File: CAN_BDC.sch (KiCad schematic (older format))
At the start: 27 parts, among them P1 CONN_01X02, P2 CONN_01X05, P3 CONN_01X02, P4 CONN_01X04, P5 CONN_01X04, P6 CONN_01X02, P7 CONN_01X04, P8 CONN_01X04, P9 CONN_01X02, U1 PSD2CAN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

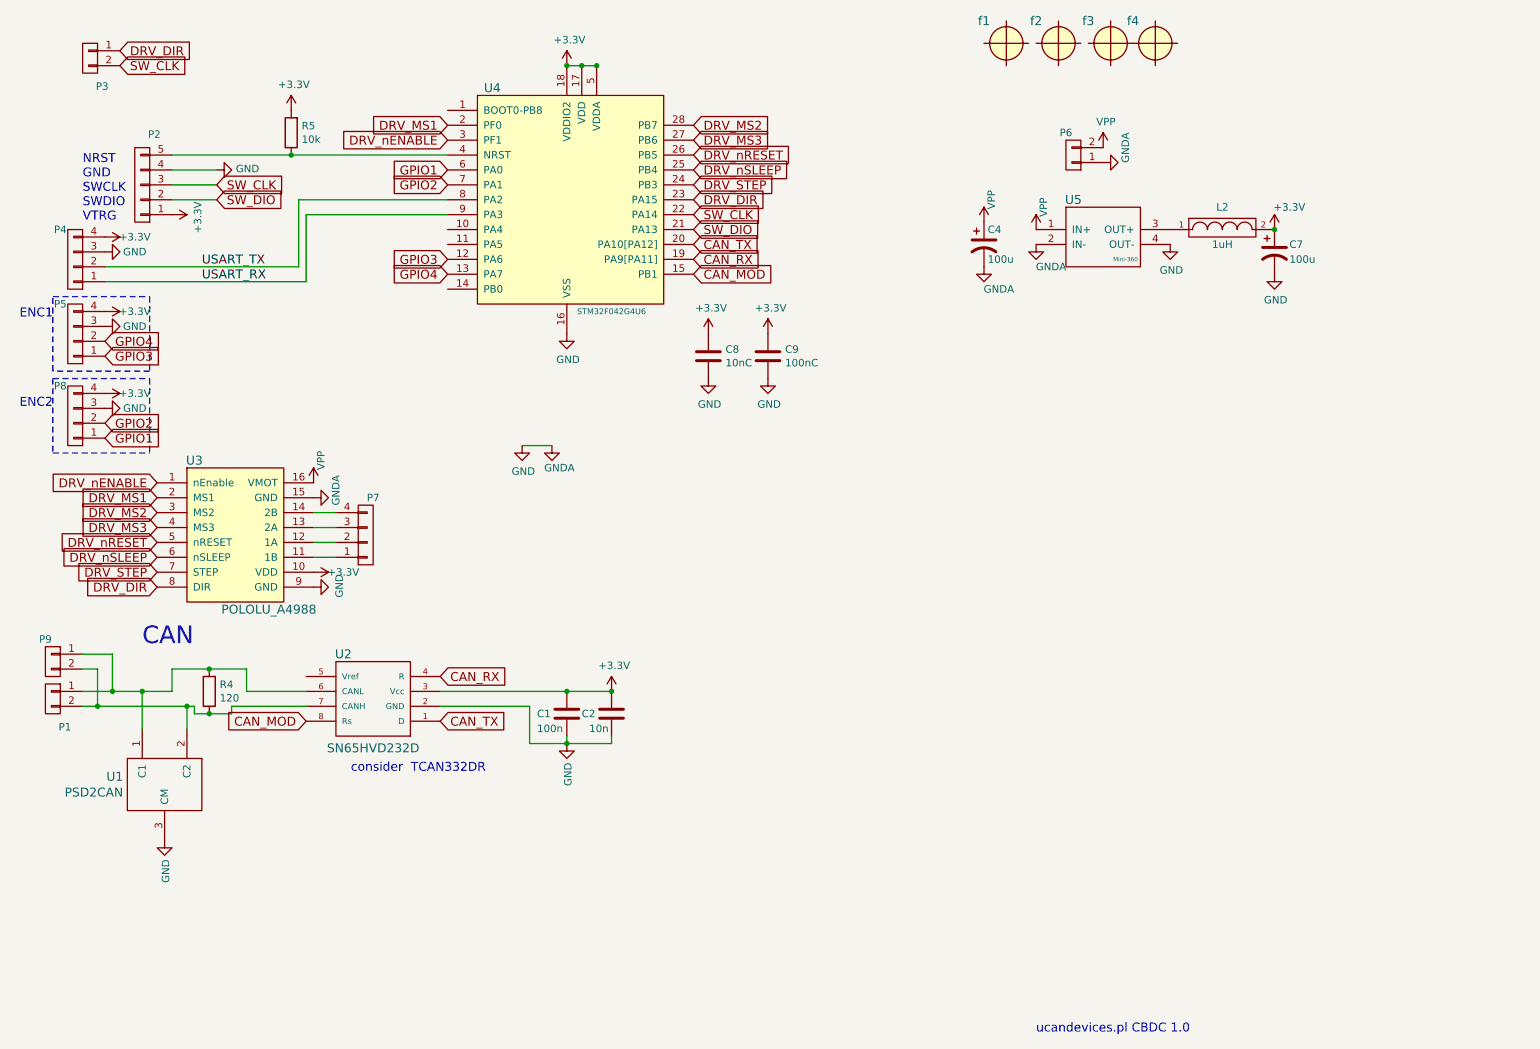
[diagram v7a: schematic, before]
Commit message: DRV8825 and DRV8801 solder pads addition
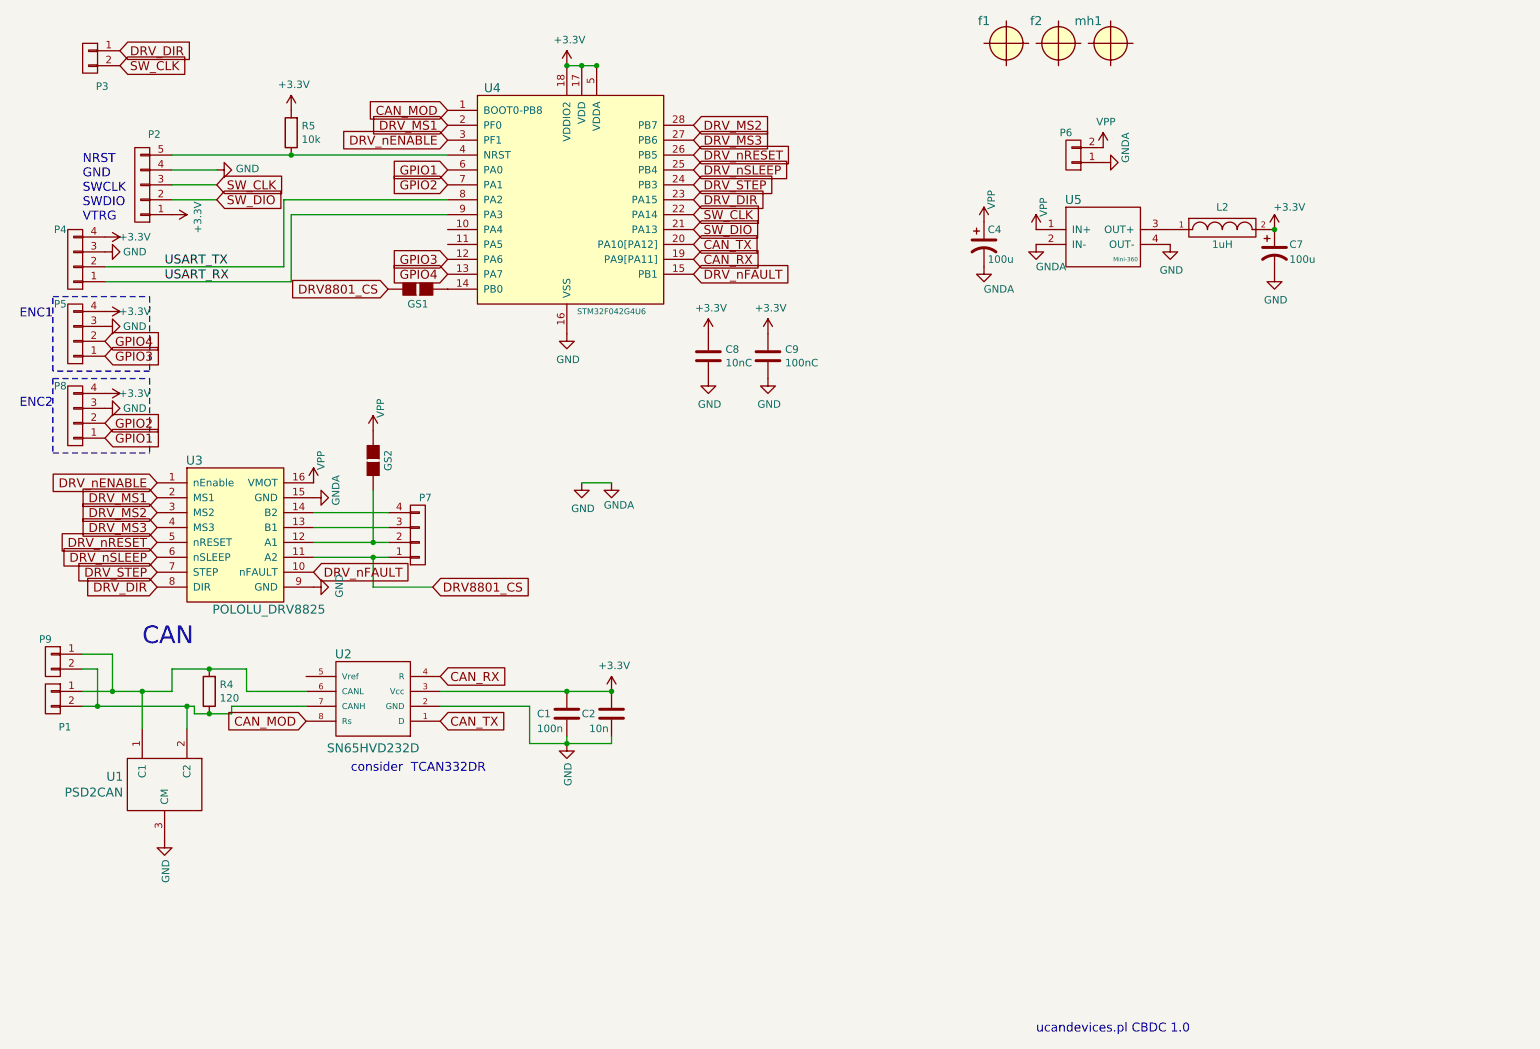
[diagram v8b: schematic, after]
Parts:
- removed U3: POLOLU_A4988, usb_ccb_custom:POLOLU_A4988, symbol POLOLU_A4988
- removed f4: fiducial, Fiducials:Fiducial_1mm_Dia_2.54mm_Outer_CopperBottom, symbol fiducial
- added GS1, GS2: GS2, Connect:GS2, symbol GS2
- added U3: POLOLU_DRV8825, usb_ccb_custom:POLOLU_A4988, symbol POLOLU_DRV8825
- mh1: renamed from f3; footprint Fiducials:Fiducial_1mm_Dia_2.54mm_Outer_CopperBottom -> usb_ccb_custom:1pin
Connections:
- net CAN_MOD: now also U4.1 (BOOT0-PB8); no longer U4.15 (PB1)
- net DRV_DIR: now also U3.8 (DIR)
- net DRV_MS1: now also U3.2 (MS1)
- net DRV_MS2: now also U3.3 (MS2)
- net DRV_MS3: now also U3.4 (MS3)
- net DRV_STEP: now also U3.7 (STEP)
- net DRV_nENABLE: now also U3.1 (nEnable)
- net DRV_nRESET: now also U3.5 (nRESET)
- net DRV_nSLEEP: now also U3.6 (nSLEEP)
- net GND: now also U3.15 (GND), U3.9 (GND)
- net VPP: now also GS2.1 (G1), U3.16 (VMOT)
- net at U4.14 (PB0): now also GS1.1 (G1)
- net DRV8801_CS: now reaches P7.1 (P1)
- net DRV8801_CS: now also GS1.2 (G2), U3.11 (A2)
- net at P7.2 (P2): now also GS2.2 (G2), U3.12 (A1)
- net at P7.3 (P3): now also U3.13 (B1)
- net at P7.4 (P4): now also U3.14 (B2)
- new net DRV_nFAULT: U3.10 (nFAULT), U4.15 (PB1)
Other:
- moved on the sheet: P7
